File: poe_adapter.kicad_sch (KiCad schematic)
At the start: 9 parts

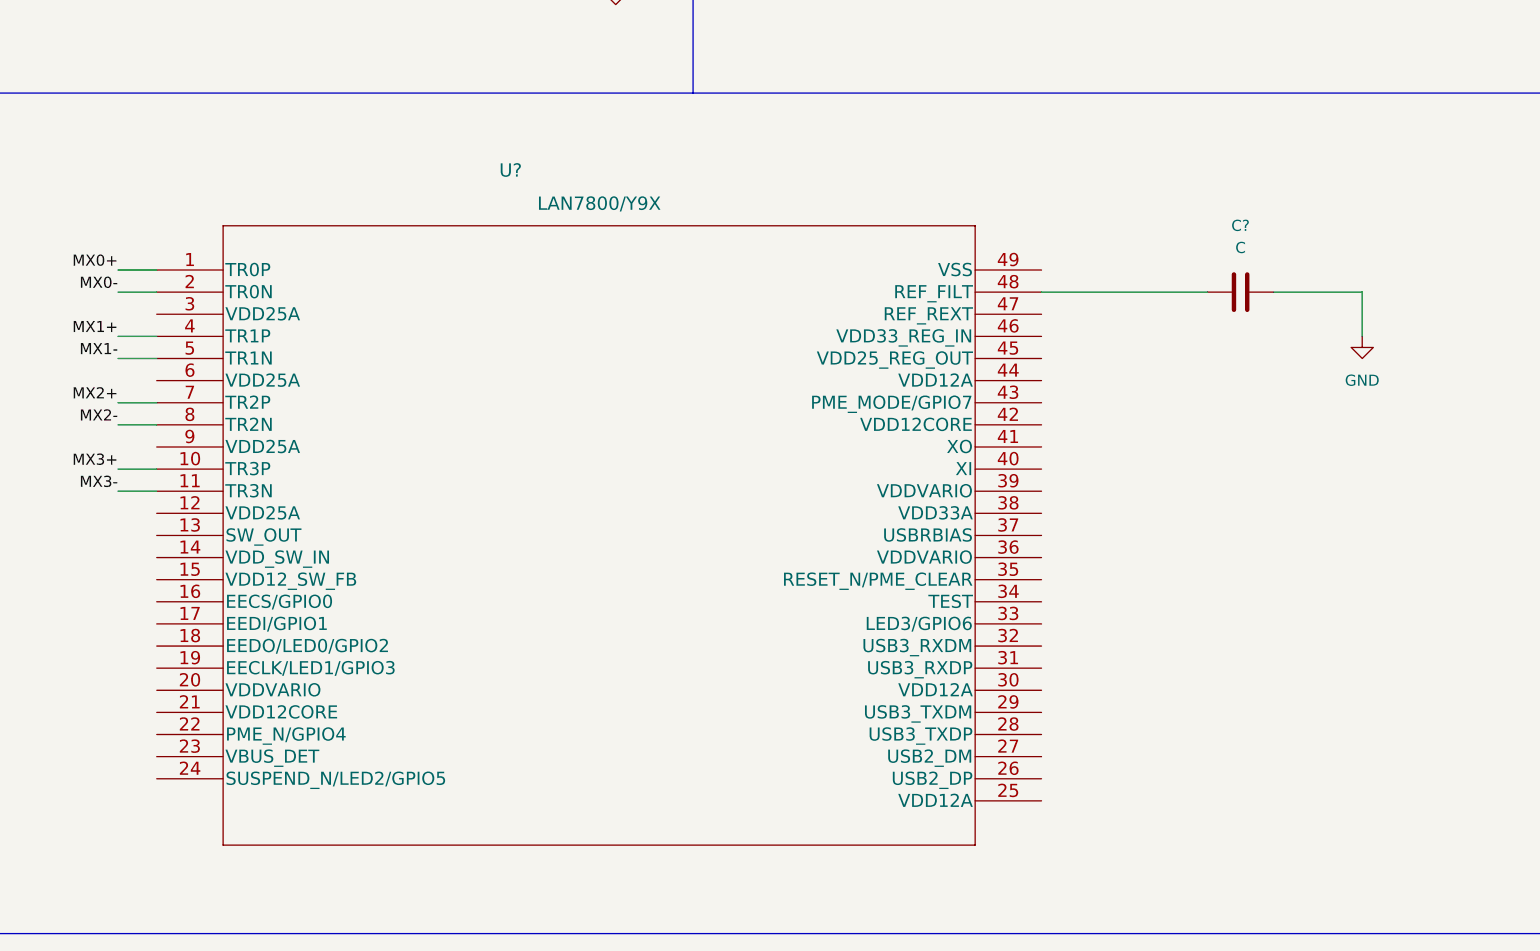
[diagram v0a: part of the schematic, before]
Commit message: LAN7800 Update 220707
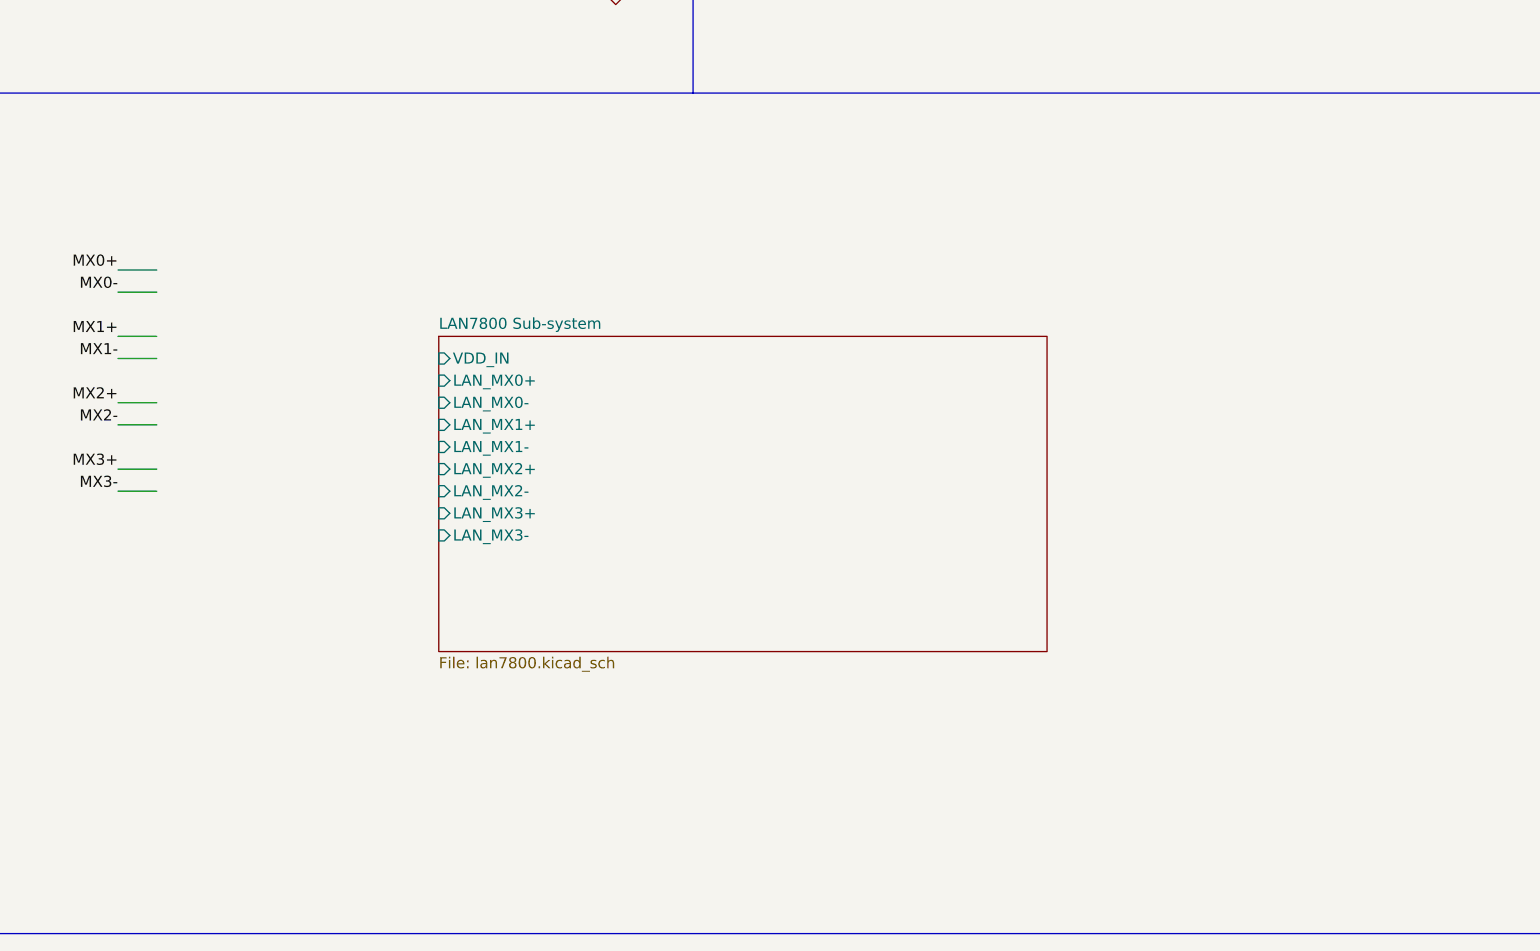
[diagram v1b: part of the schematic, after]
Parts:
- removed C?: C, symbol Device:C
- removed U?: LAN7800/Y9X, SQFN48_7X7_Y9X_MCH, symbol Microchip:LAN7800/Y9X
- P?: footprint (none) -> Connector_USB:USB_C_Plug_Molex_105444
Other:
- added sheet LAN7800 Sub-system (lan7800.kicad_sch)
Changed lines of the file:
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@@
-    (stroke (width 0) (type default) (color 0 0 0 0))
-  )
-  (wire (pts (xy 260.35 99.06) (xy 260.35 104.14))
     (stroke (width 0) (type default) (color 0 0 0 0))
   )
@@
     (stroke (width 0) (type default) (color 0 0 0 0))
   )
-  (wire (pts (xy 223.52 99.06) (xy 242.57 99.06))
-    (stroke (width 0) (type default) (color 0 0 0 0))
-  )
   (wire (pts (xy 118.11 36.83) (xy 121.92 36.83))
     (stroke (width 0) (type default) (color 0 0 0 0))
@@
   )
   (wire (pts (xy 60.325 144.145) (xy 57.15 144.145))
-    (stroke (width 0) (type default) (color 0 0 0 0))
-  )
-  (wire (pts (xy 250.19 99.06) (xy 260.35 99.06))
     (stroke (width 0) (type default) (color 0 0 0 0))
   )
@@
     (pin "9")
   )
-  (symbol (lib_id "power:GND") (at 260.35 104.14 0) (unit 1)
-    (in_bom yes) (on_board yes) (fields_autoplaced)
-    (property "Reference" "#PWR?" (id 0) (at 260.35 110.49 0)
-      (effects (font (size 1.27 1.27)) hide)
-    )
-    (property "Value" "GND" (id 1) (at 260.35 109.22 0))
-    (property "Footprint" "" (id 2) (at 260.35 104.14 0)
-      (effects (font (size 1.27 1.27)) hide)
-    )
-    (property "Datasheet" "" (id 3) (at 260.35 104.14 0)
-      (effects (font (size 1.27 1.27)) hide)
-    )
-    (pin "1")
-  )
   (symbol (lib_id "power:GND") (at 38.1 156.21 0) (unit 1)
     (in_bom yes) (on_board yes)
@@
     )
     (pin "1")
-  )
-  (symbol (lib_id "Device:C") (at 246.38 99.06 90) (unit 1)
-    (in_bom yes) (on_board yes) (fields_autoplaced)
-    (property "Reference" "C?" (id 0) (at 246.38 91.44 90))
-    (property "Value" "C" (id 1) (at 246.38 93.98 90))
-    (property "Footprint" "" (id 2) (at 250.19 98.0948 0)
-      (effects (font (size 1.27 1.27)) hide)
-    )
-    (property "Datasheet" "~" (id 3) (at 246.38 99.06 0)
-      (effects (font (size 1.27 1.27)) hide)
-    )
-    (pin "1")
-    (pin "2")
   )
   (symbol (lib_id "power:+2V5") (at 189.23 24.765 0) (unit 1)
@@
     (property "Reference" "P?" (id 0) (at 41.91 77.47 0))
     (property "Value" "USB_C_Plug" (id 1) (at 41.91 80.01 0))
-    (property "Footprint" "" (id 2) (at 45.72 111.125 0)
+    (property "Footprint" "Connector_USB:USB_C_Plug_Molex_105444" (id 2) (at 45.72 111.125 0)
       (effects (font (size 1.27 1.27)) hide)
     )
@@
     (pin "2")
   )
-  (symbol (lib_id "Microchip:LAN7800{slash}Y9X") (at 121.92 96.52 0) (unit 1)
-    (in_bom yes) (on_board yes)
-    (property "Reference" "U?" (id 0) (at 162.56 85.09 0)
-      (effects (font (size 1.524 1.524)))
-    )
-    (property "Value" "LAN7800/Y9X" (id 1) (at 172.72 88.9 0)
-      (effects (font (size 1.524 1.524)))
-    )
-    (property "Footprint" "SQFN48_7X7_Y9X_MCH" (id 2) (at 172.72 90.424 0)
-      (effects (font (size 1.524 1.524)) hide)
-    )
-    (property "Datasheet" "https://ww1.microchip.com/downloads/aemDocuments/documents/UNG/ProductDocuments/DataSheets/LAN7800-Data-Sheet-DS00001992H.pdf" (id 3) (at 121.92 96.52 0)
-      (effects (font (size 1.524 1.524)) hide)
-    )
-    (pin "1")
-    (pin "10")
-    (pin "11")
-    (pin "12")
-    (pin "13")
-    (pin "14")
-    (pin "15")
-    (pin "16")
-    (pin "17")
-    (pin "18")
-    (pin "19")
-    (pin "2")
-    (pin "20")
-    (pin "21")
-    (pin "22")
-    (pin "23")
-    (pin "24")
-    (pin "25")
-    (pin "26")
-    (pin "27")
-    (pin "28")
-    (pin "29")
-    (pin "3")
-    (pin "30")
-    (pin "31")
-    (pin "32")
-    (pin "33")
-    (pin "34")
-    (pin "35")
-    (pin "36")
-    (pin "37")
-    (pin "38")
-    (pin "39")
-    (pin "4")
-    (pin "40")
-    (pin "41")
-    (pin "42")
-    (pin "43")
-    (pin "44")
-    (pin "45")
-    (pin "46")
-    (pin "47")
-    (pin "48")
-    (pin "49")
-    (pin "5")
-    (pin "6")
-    (pin "7")
-    (pin "8")
-    (pin "9")
-  )
   (symbol (lib_id "Connector:8P8C_LED_Shielded") (at 50.165 36.83 0) (mirror x) (unit 1)
     (in_bom yes) (on_board yes) (fields_autoplaced)
@@
     (pin "1")
   )
+  (sheet (at 154.305 104.14) (size 69.85 36.195) (fields_autoplaced)
+    (stroke (width 0.1524) (type solid) (color 0 0 0 0))
+    (fill (color 0 0 0 0.0000))
+    (property "Sheet name" "LAN7800 Sub-system" (id 0) (at 154.305 103.4284 0)
+      (effects (font (size 1.27 1.27)) (justify left bottom))
+    )
+    (property "Sheet file" "lan7800.kicad_sch" (id 1) (at 154.305 140.9196 0)
+      (effects (font (size 1.27 1.27)) (justify left top))
+    )
+    (pin "LAN_MX0+" input (at 154.305 109.22 180)
+      (effects (font (size 1.27 1.27)) (justify left))
+    )
+    (pin "LAN_MX0-" input (at 154.305 111.76 180)
+      (effects (font (size 1.27 1.27)) (justify left))
+    )
+    (pin "LAN_MX1+" input (at 154.305 114.3 180)
+      (effects (font (size 1.27 1.27)) (justify left))
+    )
+    (pin "LAN_MX1-" input (at 154.305 116.84 180)
+      (effects (font (size 1.27 1.27)) (justify left))
+    )
+    (pin "LAN_MX2+" input (at 154.305 119.38 180)
+      (effects (font (size 1.27 1.27)) (justify left))
+    )
+    (pin "LAN_MX2-" input (at 154.305 121.92 180)
+      (effects (font (size 1.27 1.27)) (justify left))
+    )
+    (pin "LAN_MX3+" input (at 154.305 124.46 180)
+      (effects (font (size 1.27 1.27)) (justify left))
+    )
+    (pin "LAN_MX3-" input (at 154.305 127 180)
+      (effects (font (size 1.27 1.27)) (justify left))
+    )
+    (pin "VDD_IN" input (at 154.305 106.68 180)
+      (effects (font (size 1.27 1.27)) (justify left))
+    )
+  )
   (sheet_instances
     (path "/" (page "1"))
+    (path "/9d43f031-4287-4645-997e-8ec53611a4dd" (page "2"))
   )
   (symbol_instances
-    (path "/0d3b042d-453f-46d5-bd00-1de43502bade"
-      (reference "#PWR?") (unit 1) (value "GND") (footprint "")
+    (path "/9d43f031-4287-4645-997e-8ec53611a4dd/0800fca6-7b16-4bd3-ad19-2ee08b9816ec"
+      (reference "#PWR?") (unit 1) (value "+1V2") (footprint "")
+    )
+    (path "/9d43f031-4287-4645-997e-8ec53611a4dd/0c578556-e65e-4d40-b26b-1f2323dc5c25"
+      (reference "#PWR?") (unit 1) (value "VSS") (footprint "")
     )
     (path "/13289c47-db8d-4343-8234-520051bc2616"
@@
       (reference "#PWR?") (unit 1) (value "GND") (footprint "")
     )
+    (path "/9d43f031-4287-4645-997e-8ec53611a4dd/20eddc41-91c2-43e6-ba45-9e2c2cb0f8d9"
+      (reference "#PWR?") (unit 1) (value "VSS") (footprint "")
+    )
+    (path "/9d43f031-4287-4645-997e-8ec53611a4dd/2d96a198-433c-4931-8d57-9b1c4994818a"
+      (reference "#PWR?") (unit 1) (value "VSS") (footprint "")
+    )
+    (path "/9d43f031-4287-4645-997e-8ec53611a4dd/3e499563-6c0d-40f7-97d7-784a6998356a"
+      (reference "#PWR?") (unit 1) (value "+1V2") (footprint "")
+    )
     (path "/55cdfa96-cd8a-4907-b528-009453147325"
       (reference "#PWR?") (unit 1) (value "+2V5") (footprint "")
@@
       (reference "#PWR?") (unit 1) (value "+3V3") (footprint "")
     )
+    (path "/9d43f031-4287-4645-997e-8ec53611a4dd/78027ec0-c473-40e3-924d-c5e0d19a55e5"
+      (reference "#PWR?") (unit 1) (value "+1V2") (footprint "")
+    )
+    (path "/9d43f031-4287-4645-997e-8ec53611a4dd/78cd1967-f007-409e-b00d-539c03b4ed78"
+      (reference "#PWR?") (unit 1) (value "+1V2") (footprint "")
+    )
     (path "/7aa31451-4668-4578-a3e3-20bf3059b5e3"
       (reference "#PWR?") (unit 1) (value "GND") (footprint "")
     )
+    (path "/9d43f031-4287-4645-997e-8ec53611a4dd/8223675b-b650-4c0e-a7ef-a78ca7aa93ce"
+      (reference "#PWR?") (unit 1) (value "+1V2") (footprint "")
+    )
+    (path "/9d43f031-4287-4645-997e-8ec53611a4dd/af0c677e-2299-4b4d-8944-5b63a4939113"
+      (reference "#PWR?") (unit 1) (value "+1V2") (footprint "")
+    )
     (path "/e32d7b03-9687-4ea9-ad22-680fb9676a7e"
       (reference "#PWR?") (unit 1) (value "GND") (footprint "")
@@
       (reference "C?") (unit 1) (value "100nF") (footprint "")
     )
-    (path "/27469c1c-3e44-4f65-a64b-688e61d61250"
-      (reference "C?") (unit 1) (value "C") (footprint "")
-    )
     (path "/55d13134-88c4-464b-92e7-8a4de99c8534"
       (reference "C?") (unit 1) (value "100nF") (footprint "")
@@
       (reference "C?") (unit 1) (value "100nF") (footprint "")
     )
+    (path "/9d43f031-4287-4645-997e-8ec53611a4dd/d18b2358-bda7-4211-aadd-e4cc0795a304"
+      (reference "C?") (unit 1) (value "1uF") (footprint "")
+    )
+    (path "/9d43f031-4287-4645-997e-8ec53611a4dd/f5dc5861-d352-4df0-90ef-b87458689c6d"
+      (reference "C?") (unit 1) (value "10uF") (footprint "")
+    )
     (path "/d4907967-024d-443f-bd57-a3f346e85e67"
       (reference "J?") (unit 1) (value "8P8C_LED_Shielded") (footprint "")
     )
+    (path "/9d43f031-4287-4645-997e-8ec53611a4dd/f8ae138d-89df-43ef-9940-304bec57cf28"
+      (reference "L?") (unit 1) (value "3.3uH") (footprint "")
+    )
     (path "/8bed02aa-e2e3-4396-9a31-e4ce1fba3996"
       (reference "P?") (unit 1) (value "USB_C_Plug") (footprint "Connector_USB:USB_C_Plug_Molex_105444")
     )
+    (path "/9d43f031-4287-4645-997e-8ec53611a4dd/3a6394ad-8e1d-4c64-98ae-3a5e26e324fe"
+      (reference "R?") (unit 1) (value "2k") (footprint "")
+    )
+    (path "/9d43f031-4287-4645-997e-8ec53611a4dd/46e7fa13-5605-450d-ae06-ae8fe83bc34e"
+      (reference "R?") (unit 1) (value "12k") (footprint "")
+    )
     (path "/02e3c308-64f1-4854-97c3-314235fa8339"
       (reference "TR?") (unit 1) (value "TG111-MSC13LF") (footprint "Transformer_SMD:Transformer_Ethernet_HALO_TG111-MSC13")
     )
-    (path "/ad204674-31bc-4b11-a857-8cf5b0b2e8e4"
+    (path "/9d43f031-4287-4645-997e-8ec53611a4dd/e839030f-3630-4679-abd4-0628298cf701"
       (reference "U?") (unit 1) (value "LAN7800/Y9X") (footprint "SQFN48_7X7_Y9X_MCH")
     )

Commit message: LAN7800 Update 220707-2
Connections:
- net MX0- is gone; now on net MX0+: TR?.11 (TD4+)
- net MX1+ is gone; now on net MX0+: TR?.9 (TD3-)
- net MX1- is gone; now on net MX0+: TR?.8 (TD3+)
- net MX2+ is gone; now on net MX0+: TR?.6 (TD2-)
- net MX2- is gone; now on net MX0+: TR?.5 (TD2+)
- net MX3+ is gone; now on net MX0+: TR?.3 (TD1-)
- net MX3- is gone; now on net MX0+: TR?.2 (TD1+)
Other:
- sheet LAN7800 Sub-system ports: added 3V3, VSS_IN; removed none
- note added: "1V8-3V3"
- note added: "GND"

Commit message: LAN7800 update 0710
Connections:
- net MX0+: no longer TR?.11 (TD4+), TR?.2 (TD1+), TR?.3 (TD1-), TR?.5 (TD2+), TR?.6 (TD2-), TR?.8 (TD3+), TR?.9 (TD3-)
- new net MX0-: TR?.11 (TD4+)
- new net MX1+: TR?.9 (TD3-)
- new net MX1-: TR?.8 (TD3+)
- new net MX2+: TR?.6 (TD2-)
- new net MX2-: TR?.5 (TD2+)
- new net MX3+: TR?.3 (TD1-)
- new net MX3-: TR?.2 (TD1+)
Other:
- sheet LAN7800 Sub-system ports: added 3V3_Board, USB2_DM, USB2_DP, USB3_RXDM, USB3_RXDP, USB3_TXDM, USB3_TXDP; removed 3V3
- note added: "1V8-3V3 Input"
- note added: "3V3 Input"
- note removed: "1V8-3V3"

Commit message: finish datalink
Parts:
- removed J?: 8P8C_LED_Shielded, symbol Connector:8P8C_LED_Shielded
- added C? (x3): 0.1uF, symbol Device:C_Small
- added C?: 1nF, symbol Device:C_Small
- added J?: RJ45_LED_Shielded, symbol Connector:RJ45_LED_Shielded
- added R?: 330R, symbol Device:R_Small
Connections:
- net GND: now also C?.2, C?.2, J?.10, J?.11, R?.2; no longer P?.S1 (SHIELD)
- net LAN7800 Sub-system/USB3_TXDM: now also C?.1
- net LAN7800 Sub-system/USB3_TXDP: now also C?.1
- net RJ45_DA+: now also J?.8
- net RJ45_DA-: now also J?.7
- net RJ45_DB+: now also J?.6
- net RJ45_DB-: now also J?.3
- net RJ45_DC+: now also J?.5
- net RJ45_DC-: now also J?.4
- net RJ45_DD+: now also J?.2
- net RJ45_DD-: now also J?.1
- net RJ45_LED1: now also J?.12
- net RJ45_LED2: now also J?.9
- net USB_RX1+: now also C?.2
- net USB_RX1-: now also C?.2
- net USB_RX2+: no longer names the net of P?.A11 (RX2+)
- net USB_RX2-: no longer names the net of P?.A10 (RX2-)
- net USB_TX2+: no longer names the net of P?.B2 (TX2+)
- net USB_TX2-: no longer names the net of P?.B3 (TX2-)
- new net Earth_Protective: C?.1, C?.1, J?.SH, P?.S1 (SHIELD), R?.1
- no-connect marks 0 -> 4
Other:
- sheet LAN7800 Sub-system ports: added LED2, LED3, VDD_IO_IN; removed VDD_IN
- note added: "ESD Protection"

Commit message: led update
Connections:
- net +3V3: now also J?.10, J?.12
- net GND: no longer J?.10, J?.11
- net RJ45_LED1: now also J?.11; no longer J?.12
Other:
- note added: "Ethernet to USB SuperSpeed"
- moved on the sheet: C?, TR?

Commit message: change 20220714, update datalink
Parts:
- removed C? (x2): 0.1uF, symbol Device:C_Small
- added C? (x2): 0.1uF, symbol Device:C_Small
- added R? (x2): 0Ω, symbol Device:R_Small
- C?: Voltage (none) -> 2kV
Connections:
- net USB_D+: now also R?.2; no longer P?.A6 (D+)
- net USB_D-: now also R?.2; no longer P?.A7 (D-)
- net USB_RX1+: now also C?.2; no longer P?.B11 (RX1+)
- net USB_RX1-: now also C?.2; no longer P?.B10 (RX1-)
- new net: C?.1, P?.B11 (RX1+)
- new net: P?.A6 (D+), R?.1
- new net: C?.1, P?.B10 (RX1-)
- new net: P?.A7 (D-), R?.1
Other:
- note added: "CC USED FOR USB-PD"
- note added: "LOW SPEED LINK"
- note added: "USE 15Ω IF NECESSARY"
- moved on the sheet: C?, P?, R?
